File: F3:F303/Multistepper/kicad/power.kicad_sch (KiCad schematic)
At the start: 26 parts, among them J10 Screw_Terminal_01x02, Q2 IRF9310, U4 LM4050A(b)EX3-3.3, U5 LM2576-5.0, U6 LM1117-3.3

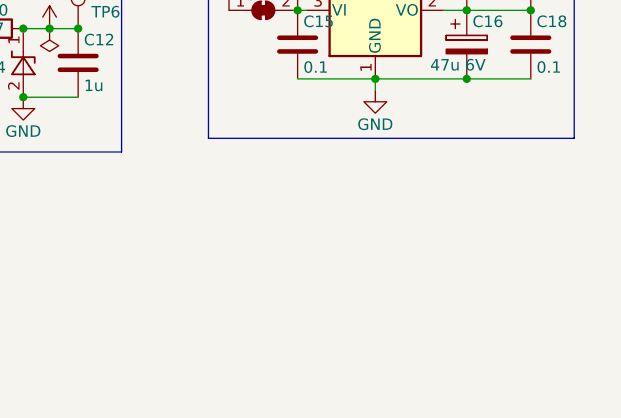
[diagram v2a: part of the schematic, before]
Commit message: Multistepper PCB almost ready
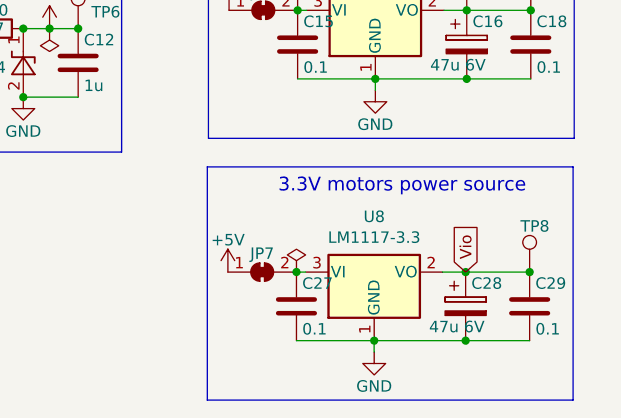
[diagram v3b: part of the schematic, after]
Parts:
- added C27, C29: 0.1, Capacitor_SMD:C_0603_1608Metric_Pad1.08x0.95mm_HandSolder, symbol stm32-rescue:C
- added C28: 47u 6V, Capacitor_Tantalum_SMD:CP_EIA-3216-18_Kemet-A_Pad1.58x1.35mm_HandSolder, symbol stm32-rescue:CP
- added JP7: Vio, Jumper:SolderJumper-2_P1.3mm_Open_TrianglePad1.0x1.5mm, symbol Jumper:SolderJumper_2_Bridged
- added TP8: Vio, TestPoint:TestPoint_THTPad_1.5x1.5mm_Drill0.7mm, symbol Connector:TestPoint
- added U8: LM1117-3.3, Package_TO_SOT_SMD:SOT-223-3_TabPin2, symbol Regulator_Linear:LM1117-3.3
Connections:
- net +5V: now also JP7.1 (A)
- net GND: now also C27.2, C28.2, C29.2, U8.1 (GND)
- new net: C27.1, JP7.2 (B), U8.3 (VI)
- new net Vio: C28.1, C29.1, TP8.1, U8.2 (VO)
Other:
- note added: "3.3V motors power source"
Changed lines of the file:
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@@
 (kicad_sch (version 20211123) (generator eeschema)
   (paper "A4")
+  (junction (at 101.727 100.965) (diameter 0) (color 0 0 0 0)
+  )
+  (junction (at 84.455 108.585) (diameter 0) (color 0 0 0 0)
+  )
   (junction (at 39.878 36.068) (diameter 0) (color 0 0 0 0)
   )
@@
   (junction (at 45.212 36.068) (diameter 0) (color 0 0 0 0)
   )
+  (junction (at 94.615 100.965) (diameter 0) (color 0 0 0 0)
+  )
   (junction (at 94.996 48.768) (diameter 0) (color 0 0 0 0)
   )
@@
   (junction (at 45.466 81.534) (diameter 0) (color 0 0 0 0)
   )
+  (junction (at 94.615 108.585) (diameter 0) (color 0 0 0 0)
+  )
   (junction (at 69.85 52.578) (diameter 0) (color 0 0 0 0)
   )
@@
   (junction (at 48.514 43.688) (diameter 0) (color 0 0 0 0)
   )
+  (junction (at 75.819 100.965) (diameter 0) (color 0 0 0 0)
+  )
   (junction (at 94.996 28.448) (diameter 0) (color 0 0 0 0)
   )
@@
     (stroke (width 0) (type default) (color 0 0 0 0))
   )
+  (wire (pts (xy 84.455 108.585) (xy 94.615 108.585))
+    (stroke (width 0) (type default) (color 0 0 0 0))
+  )
   (wire (pts (xy 48.514 43.688) (xy 51.816 43.688))
     (stroke (width 0) (type default) (color 0 0 0 0))
@@
     (stroke (width 0) (type default) (color 0 0 0 0))
   )
+  (polyline (pts (xy 106.553 115.189) (xy 106.553 89.281))
+    (stroke (width 0) (type default) (color 0 0 0 0))
+  )
+  (polyline (pts (xy 65.913 89.281) (xy 65.913 115.189))
+    (stroke (width 0) (type default) (color 0 0 0 0))
+  )
   (polyline (pts (xy 21.59 87.63) (xy 56.388 87.63))
     (stroke (width 0) (type default) (color 0 0 0 0))
   )
+  (wire (pts (xy 76.835 100.965) (xy 75.819 100.965))
+    (stroke (width 0) (type default) (color 0 0 0 0))
+  )
+  (wire (pts (xy 84.455 109.855) (xy 84.455 108.585))
+    (stroke (width 0) (type default) (color 0 0 0 0))
+  )
+  (wire (pts (xy 101.727 100.965) (xy 94.615 100.965))
+    (stroke (width 0) (type default) (color 0 0 0 0))
+  )
   (wire (pts (xy 75.946 79.502) (xy 84.582 79.502))
     (stroke (width 0) (type default) (color 0 0 0 0))
   )
+  (wire (pts (xy 101.727 108.585) (xy 94.615 108.585))
+    (stroke (width 0) (type default) (color 0 0 0 0))
+  )
   (wire (pts (xy 94.996 41.148) (xy 94.996 36.068))
     (stroke (width 0) (type default) (color 0 0 0 0))
   )
+  (wire (pts (xy 75.819 108.585) (xy 84.455 108.585))
+    (stroke (width 0) (type default) (color 0 0 0 0))
+  )
   (wire (pts (xy 45.466 73.914) (xy 48.387 73.914))
     (stroke (width 0) (type default) (color 0 0 0 0))
@@
     (stroke (width 0) (type default) (color 0 0 0 0))
   )
+  (polyline (pts (xy 65.913 115.189) (xy 106.553 115.189))
+    (stroke (width 0) (type default) (color 0 0 0 0))
+  )
+  (polyline (pts (xy 106.553 89.281) (xy 65.913 89.281))
+    (stroke (width 0) (type default) (color 0 0 0 0))
+  )
   (wire (pts (xy 29.464 29.464) (xy 32.258 29.464))
     (stroke (width 0) (type default) (color 0 0 0 0))
@@
   )
   (wire (pts (xy 84.582 80.772) (xy 84.582 79.502))
+    (stroke (width 0) (type default) (color 0 0 0 0))
+  )
+  (wire (pts (xy 92.075 100.965) (xy 94.615 100.965))
     (stroke (width 0) (type default) (color 0 0 0 0))
   )
@@
   (text "12..24Vin" (at 27.432 20.32 0)
     (effects (font (size 1.27 1.27)) (justify left bottom))
+  )
+  (text "3.3V motors power source" (at 73.787 92.329 0)
+    (effects (font (size 1.524 1.524)) (justify left bottom))
+  )
+  (global_label "Vio" (shape input) (at 94.615 100.965 90) (fields_autoplaced)
+    (effects (font (size 1.27 1.27)) (justify left))
+    (property "Intersheet References" "${INTERSHEET_REFS}" (id 0) (at 94.5356 95.7095 90)
+      (effects (font (size 1.27 1.27)) (justify left) hide)
+    )
   )
   (symbol (lib_id "elements:IRF9310") (at 37.338 29.464 0) (unit 1)
@@
     (pin "2")
   )
+  (symbol (lib_id "stm32-rescue:C") (at 75.819 104.775 0) (unit 1)
+    (in_bom yes) (on_board yes)
+    (property "Reference" "C27" (id 0) (at 76.454 102.235 0)
+      (effects (font (size 1.27 1.27)) (justify left))
+    )
+    (property "Value" "0.1" (id 1) (at 76.454 107.315 0)
+      (effects (font (size 1.27 1.27)) (justify left))
+    )
+    (property "Footprint" "Capacitor_SMD:C_0603_1608Metric_Pad1.08x0.95mm_HandSolder" (id 2) (at 76.7842 108.585 0)
+      (effects (font (size 1.27 1.27)) hide)
+    )
+    (property "Datasheet" "" (id 3) (at 75.819 104.775 0))
+    (pin "1")
+    (pin "2")
+  )
   (symbol (lib_id "Reference_Voltage:LM4040DBZ-3") (at 45.466 77.724 90) (unit 1)
     (in_bom yes) (on_board yes)
@@
     (pin "2")
   )
+  (symbol (lib_id "power:GND") (at 84.455 109.855 0) (unit 1)
+    (in_bom yes) (on_board yes)
+    (property "Reference" "#PWR061" (id 0) (at 84.455 116.205 0)
+      (effects (font (size 1.27 1.27)) hide)
+    )
+    (property "Value" "GND" (id 1) (at 84.455 113.665 0))
+    (property "Footprint" "" (id 2) (at 84.455 109.855 0)
+      (effects (font (size 1.27 1.27)) hide)
+    )
+    (property "Datasheet" "" (id 3) (at 84.455 109.855 0)
+      (effects (font (size 1.27 1.27)) hide)
+    )
+    (pin "1")
+  )
+  (symbol (lib_id "power:PWR_FLAG") (at 75.819 100.965 0) (unit 1)
+    (in_bom yes) (on_board yes) (fields_autoplaced)
+    (property "Reference" "#FLG04" (id 0) (at 75.819 99.06 0)
+      (effects (font (size 1.27 1.27)) hide)
+    )
+    (property "Value" "PWR_FLAG" (id 1) (at 75.819 97.3892 0)
+      (effects (font (size 1.27 1.27)) hide)
+    )
+    (property "Footprint" "" (id 2) (at 75.819 100.965 0)
+      (effects (font (size 1.27 1.27)) hide)
+    )
+    (property "Datasheet" "~" (id 3) (at 75.819 100.965 0)
+      (effects (font (size 1.27 1.27)) hide)
+    )
+    (pin "1")
+  )
+  (symbol (lib_id "stm32-rescue:+5V") (at 68.199 100.965 0) (unit 1)
+    (in_bom yes) (on_board yes)
+    (property "Reference" "#PWR037" (id 0) (at 68.199 104.775 0)
+      (effects (font (size 1.27 1.27)) hide)
+    )
+    (property "Value" "+5V" (id 1) (at 68.199 97.409 0))
+    (property "Footprint" "" (id 2) (at 68.199 100.965 0))
+    (property "Datasheet" "" (id 3) (at 68.199 100.965 0))
+    (pin "1")
+  )
   (symbol (lib_id "Device:C_Polarized") (at 94.996 44.958 0) (unit 1)
     (in_bom yes) (on_board yes)
@@
     (pin "4")
     (pin "5")
+  )
+  (symbol (lib_id "Jumper:SolderJumper_2_Bridged") (at 72.009 100.965 0) (unit 1)
+    (in_bom yes) (on_board yes) (fields_autoplaced)
+    (property "Reference" "JP7" (id 0) (at 72.009 98.9132 0))
+    (property "Value" "Vio" (id 1) (at 72.009 98.9131 0)
+      (effects (font (size 1.27 1.27)) hide)
+    )
+    (property "Footprint" "Jumper:SolderJumper-2_P1.3mm_Open_TrianglePad1.0x1.5mm" (id 2) (at 72.009 100.965 0)
+      (effects (font (size 1.27 1.27)) hide)
+    )
+    (property "Datasheet" "~" (id 3) (at 72.009 100.965 0)
+      (effects (font (size 1.27 1.27)) hide)
+    )
+    (pin "1")
+    (pin "2")
   )
   (symbol (lib_id "stm32-rescue:+5V") (at 68.326 71.882 0) (unit 1)
@@
     (pin "1")
   )
+  (symbol (lib_id "Connector:TestPoint") (at 101.727 100.965 0) (unit 1)
+    (in_bom yes) (on_board yes)
+    (property "Reference" "TP8" (id 0) (at 100.711 95.885 0)
+      (effects (font (size 1.27 1.27)) (justify left))
+    )
+    (property "Value" "Vio" (id 1) (at 100.203 95.631 0)
+      (effects (font (size 1.27 1.27)) (justify left) hide)
+    )
+    (property "Footprint" "TestPoint:TestPoint_THTPad_1.5x1.5mm_Drill0.7mm" (id 2) (at 106.807 100.965 0)
+      (effects (font (size 1.27 1.27)) hide)
+    )
+    (property "Datasheet" "~" (id 3) (at 106.807 100.965 0)
+      (effects (font (size 1.27 1.27)) hide)
+    )
+    (pin "1")
+  )
   (symbol (lib_id "Connector:TestPoint") (at 99.314 28.448 0) (unit 1)
     (in_bom yes) (on_board yes)
@@
     (pin "1")
   )
+  (symbol (lib_id "stm32-rescue:CP") (at 94.615 104.775 0) (unit 1)
+    (in_bom yes) (on_board yes)
+    (property "Reference" "C28" (id 0) (at 95.25 102.235 0)
+      (effects (font (size 1.27 1.27)) (justify left))
+    )
+    (property "Value" "47u 6V" (id 1) (at 90.551 107.061 0)
+      (effects (font (size 1.27 1.27)) (justify left))
+    )
+    (property "Footprint" "Capacitor_Tantalum_SMD:CP_EIA-3216-18_Kemet-A_Pad1.58x1.35mm_HandSolder" (id 2) (at 95.5802 108.585 0)
+      (effects (font (size 1.27 1.27)) hide)
+    )
+    (property "Datasheet" "" (id 3) (at 94.615 104.775 0))
+    (pin "1")
+    (pin "2")
+  )
   (symbol (lib_id "Device:C_Polarized") (at 51.816 39.878 0) (unit 1)
     (in_bom yes) (on_board yes)
@@
     (pin "3")
   )
+  (symbol (lib_id "stm32-rescue:C") (at 101.727 104.775 0) (unit 1)
+    (in_bom yes) (on_board yes)
+    (property "Reference" "C29" (id 0) (at 102.362 102.235 0)
+      (effects (font (size 1.27 1.27)) (justify left))
+    )
+    (property "Value" "0.1" (id 1) (at 102.362 107.315 0)
+      (effects (font (size 1.27 1.27)) (justify left))
+    )
+    (property "Footprint" "Capacitor_SMD:C_0603_1608Metric_Pad1.08x0.95mm_HandSolder" (id 2) (at 102.6922 108.585 0)
+      (effects (font (size 1.27 1.27)) hide)
+    )
+    (property "Datasheet" "" (id 3) (at 101.727 104.775 0))
+    (pin "1")
+    (pin "2")
+  )
   (symbol (lib_id "stm32-rescue:C") (at 75.946 75.692 0) (unit 1)
     (in_bom yes) (on_board yes)
@@
     (pin "1")
   )
+  (symbol (lib_id "Regulator_Linear:LM1117-3.3") (at 84.455 100.965 0) (unit 1)
+    (in_bom yes) (on_board yes)
+    (property "Reference" "U8" (id 0) (at 84.455 94.8182 0))
+    (property "Value" "LM1117-3.3" (id 1) (at 84.455 97.1296 0))
+    (property "Footprint" "Package_TO_SOT_SMD:SOT-223-3_TabPin2" (id 2) (at 84.455 100.965 0)
+      (effects (font (size 1.27 1.27)) hide)
+    )
+    (property "Datasheet" "http://www.ti.com/lit/ds/symlink/lm1117.pdf" (id 3) (at 84.455 100.965 0)
+      (effects (font (size 1.27 1.27)) hide)
+    )
+    (pin "1")
+    (pin "2")
+    (pin "3")
+  )
   (symbol (lib_id "power:GND") (at 94.996 48.768 0) (unit 1)
